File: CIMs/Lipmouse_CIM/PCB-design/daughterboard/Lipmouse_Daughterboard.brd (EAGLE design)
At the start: 35 x 35 mm, 13 parts

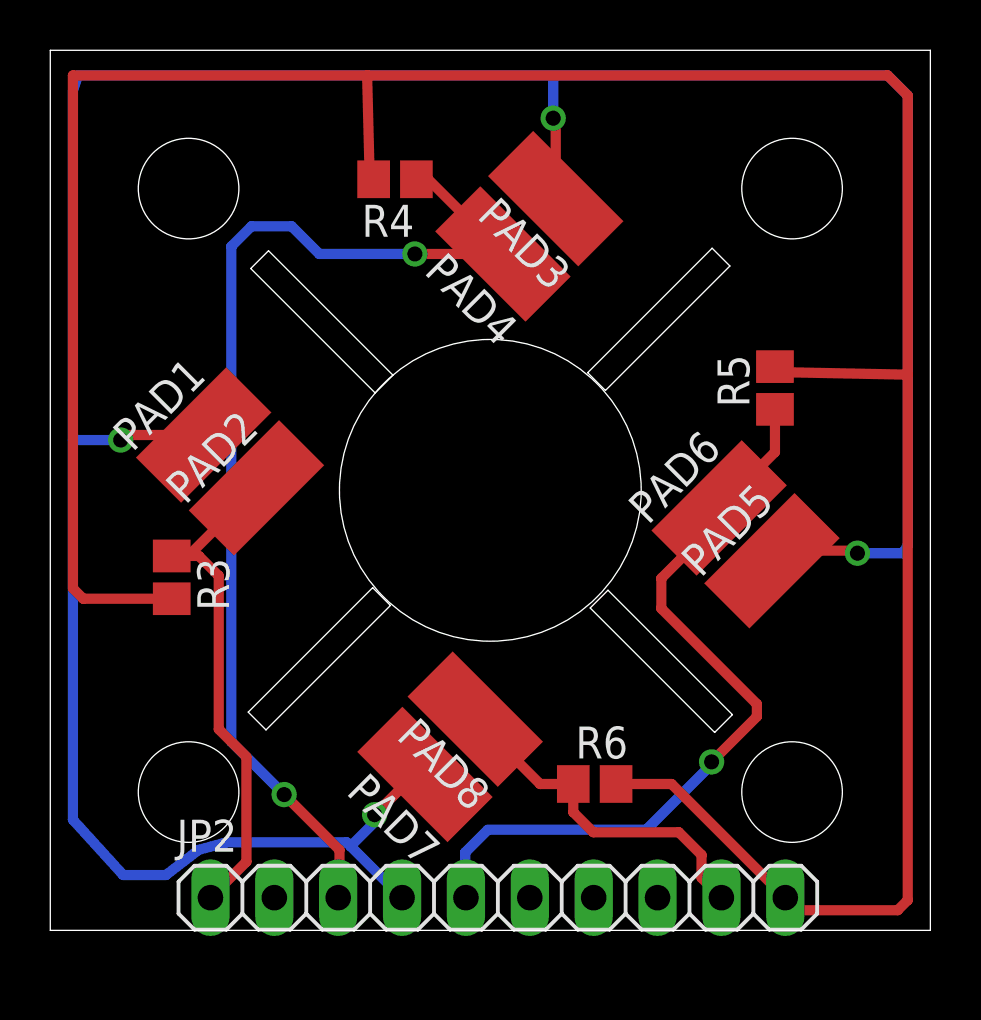
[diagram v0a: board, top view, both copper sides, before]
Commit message: Update Lipsy (Lipmouse) PCB and case designs
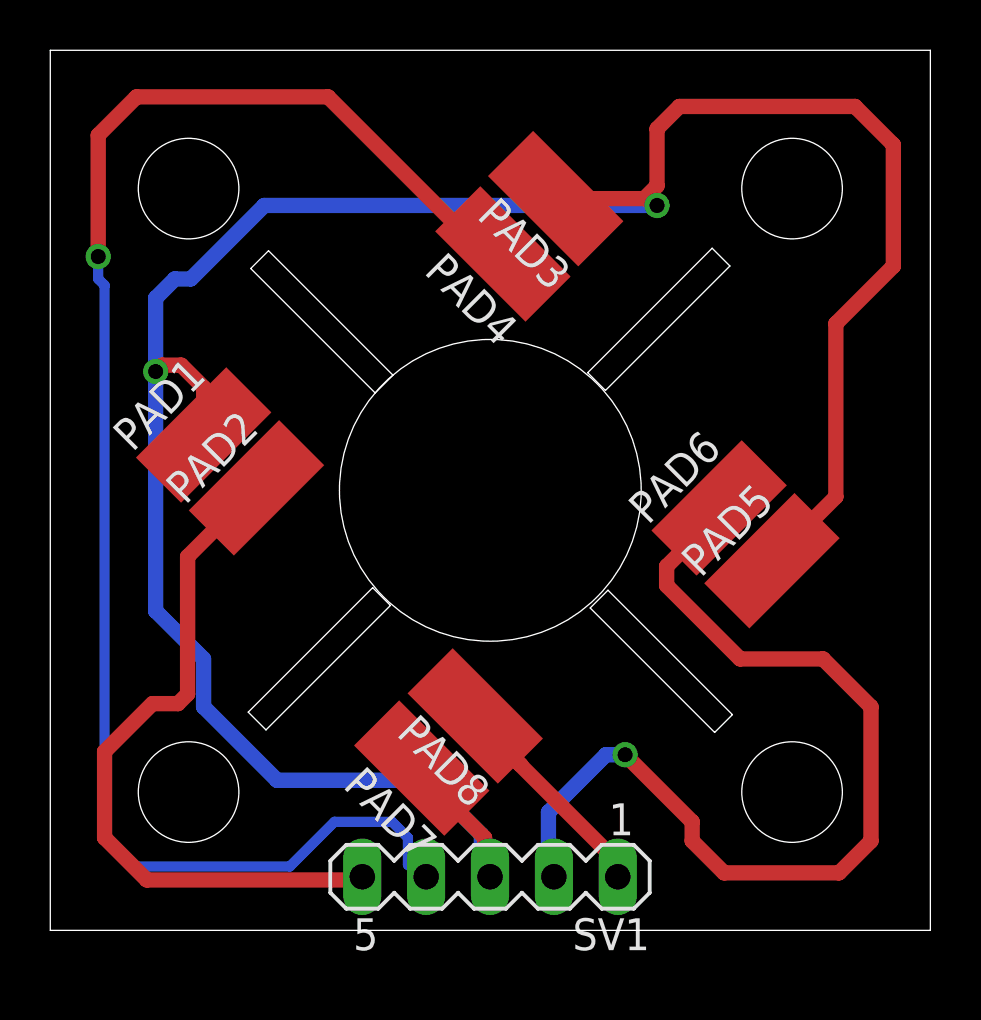
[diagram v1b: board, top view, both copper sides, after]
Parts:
- removed JP2: (no value), pinhead:1X10
- removed R3, R4, R5, R6: 10k, resistor:R0805
- added SV1: pin header, con-lstb:MA05-1
- PAD1, PAD2, PAD3, PAD4, PAD5, PAD6, PAD7, PAD8: value (none) -> solderpad
- moved PAD7 0.28 mm to (14.8, 6.45)
- moved PAD8 0.13 mm to (16.9, 8.53)
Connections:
- removed net GND: JP2.10, R3.2, R4.2, R5.2, R6.2
- net 3V3: now also SV1.3; no longer JP2.4
- net N$20: now also SV1.5; no longer JP2.1, R3.1
- net N$21: now also SV1.4; no longer JP2.3, R4.1
- net N$22: now also SV1.2; no longer JP2.5, R5.1
- net N$23: now also SV1.1; no longer JP2.9, R6.1
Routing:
- net GND: track 113.4 -> 0.00 mm
- net N$21: track 44.0 -> 62.8 mm, vias 2 -> 1
- net 3V3: track 116.0 -> 100.8 mm, vias 4 -> 2
- net N$22: track 31.4 -> 38.9 mm
- net N$20: track 20.5 -> 28.0 mm
- net N$23: track 13.9 -> 11.5 mm
